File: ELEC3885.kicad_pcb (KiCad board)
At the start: 2 copper layers, 138 x 72 mm, 35 parts, among them J1 MicInstIn, J2 LineIn, J3 HeadPhoneOut, J4 LineOutR, J5 LineOutL, J6 Conn_01x24_Female, J7 Conn_01x24_Female, U1 AP7313, U2 SGTL5000XNLA3, U3 Teensy4.1

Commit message: Initial schematic complete
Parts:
- added J8: Conn_01x06_Female, Connector_PinSocket_2.54mm:PinSocket_2x03_P2.54mm_Vertical, F.Cu at (97.3, 111.3)
- added J9: Conn_01x05_Female, Connector_PinSocket_2.54mm:PinSocket_1x05_P2.54mm_Vertical, F.Cu at (90.0, 83.0)
- added SW1: SW_Push, Button_Switch_SMD:SW_Push_1P1T_NO_6x6mm_H9.5mm, F.Cu at (117.5, 142.8)
- added SW2: SW_Push, Button_Switch_SMD:SW_Push_1P1T_NO_6x6mm_H9.5mm, F.Cu at (106.5, 142.8)
- added SW3: SW_Push, Button_Switch_SMD:SW_Push_1P1T_NO_6x6mm_H9.5mm, F.Cu at (95.6, 142.8)
- added SW4: SW_Push, Button_Switch_SMD:SW_Push_1P1T_NO_6x6mm_H9.5mm, F.Cu at (84.6, 142.8)
- U3: footprint teensy:Teensy41_no_extras -> teensy:Teensy41
- moved J1 40.9 mm to (82.0, 117.6), turned to 180 degrees
- moved H3 9.50 mm to (203.0, 141.5)
- moved H4 9.50 mm to (75.0, 141.5)
- moved U1 5.75 mm to (132.2, 110.3), turned to 90 degrees
- moved FB1 4.62 mm to (126.4, 108.6), turned to 180 degrees
- moved C10 3.03 mm to (125.0, 110.0)
- moved C7 2.09 mm to (127.2, 110.4), turned to -90 degrees
- moved C3 1.95 mm to (132.2, 107.4), turned to 180 degrees
- moved R1 1.25 mm to (130.9, 121.8)
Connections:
- net Net-(J7-Pad21) renamed /Teensy/BUTTON_0
- net Net-(J7-Pad22) renamed /Teensy/BUTTON_1
- net Net-(J7-Pad23) renamed /Teensy/BUTTON_2
- net Net-(J7-Pad24) renamed /Teensy/BUTTON_3
- J1 pad 1: unconnected-(J1-Pad1) -> GND
- J1 pad 2: unconnected-(J1-Pad2) -> Net-(J1-Pad2)
- J1 pad 3: unconnected-(J1-Pad3) -> Net-(J1-Pad3)
- J2 pad RN: GND -> /Audio/MEMS_IN
- J2 pad TN: GND -> /Audio/MEMS_IN
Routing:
- net +3.3V: track 180.5 -> 268.3 mm, vias 5 -> 10
- net /Teensy/BUTTON_3: track 8.92 -> 68.6 mm, vias 0 -> 1
- net /Teensy/BUTTON_2: track 8.92 -> 60.1 mm, vias 0 -> 1
- net /Teensy/BUTTON_1: track 8.92 -> 51.9 mm, vias 0 -> 1
- net /Audio/MEMS_IN: track 0.00 -> 40.5 mm
- net /Teensy/BUTTON_0: track 8.92 -> 43.2 mm, vias 0 -> 1
- net GND: track 11.8 -> 44.9 mm, vias 9 -> 13
- net /Audio/MIC_IN: track 13.0 -> 37.9 mm
- net /Audio/HP_VGND: track 73.1 -> 93.8 mm
- net /Audio/LINE_OUT_L: track 51.6 -> 67.5 mm, vias 2 -> 0
- net /Audio/VOLUME_CONTROL: track 84.9 -> 100.7 mm
- net Net-(J1-Pad2): track 0.00 -> 12.6 mm
- net Net-(J1-Pad3): track 0.00 -> 9.36 mm
- net /Audio/LINE_IN_L: track 46.2 -> 54.0 mm
- net /Audio/LINE_IN_R: track 50.8 -> 55.3 mm
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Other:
- board size 138 x 72 mm -> 138 x 81.5 mm
- board text added: "+"
- board text added: "+3.3"
- board text added: "+3.3V"
- board text added: "-"
- board text added: "BCLK"
- board text added: "D In"
- board text added: "D Out"
- board text added: "ECM"
- board text added: "GND"
- board text added: "HP Out"
- board text added: "In"
- board text added: "LCLK"
- board text added: "Line In"
- board text added: "Line Out L"
- board text added: "Line Out R"
- board text added: "MCLK"
- board text added: "MEMS"
- board text added: "MEMS In"
- board text added: "Mic In"
- board text added: "Mic In Breakout"
- board text added: "SCL"
- board text added: "SDA"
- board text added: "SW1"
- board text added: "SW2"
- board text added: "SW3"
- board text added: "SW4"
- board text added: "TEENSY 4.1"
- board text added: "Volume"

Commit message: New Revision
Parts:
- J8: footprint Connector_PinSocket_2.54mm:PinSocket_2x03_P2.54mm_Vertical -> Connector_PinSocket_2.54mm:PinSocket_1x06_P2.54mm_Vertical
- moved SW4 106.5 mm to (163.8, 71.5), turned to 90 degrees
- moved SW3 105.0 mm to (172.8, 71.5), turned to 90 degrees
- moved SW2 103.6 mm to (181.8, 71.5), turned to 90 degrees
- moved SW1 102.2 mm to (190.8, 71.5), turned to 90 degrees
- moved J2 82.1 mm to (84.7, 144.2), turned to 180 degrees
- moved J6 60.8 mm to (193.9, 83.6), turned to 0 degrees
- moved J3 40.1 mm to (132.5, 70.9)
- moved J4 39.9 mm to (82.6, 81.5)
- moved J5 39.9 mm to (105.8, 81.7)
- moved RV1 38.6 mm to (147.8, 78.5)
- moved J9 34.8 mm to (81.7, 116.7), turned to 90 degrees
- moved J7 34.1 mm to (160.8, 142.0), turned to 180 degrees
- moved J1 32.1 mm to (109.3, 134.4), turned to -90 degrees
- moved C14 15.9 mm to (134.4, 137.5)
- moved C6 15.9 mm to (135.5, 122.3)
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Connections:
- J1 pad 1: GND -> Net-(J1-Pad1)
- J1 pad 3: Net-(J1-Pad3) -> GND
- J7 pad 12: /Audio/VOLUME_CONTROL -> Net-(J7-Pad12)
- J7 pad 19: Net-(J7-Pad19) -> /Audio/VOLUME_CONTROL
- J8 pad 3: Net-(J1-Pad3) -> Net-(J1-Pad1)
- U3 pad 30: Net-(J7-Pad19) -> /Audio/VOLUME_CONTROL
- U3 pad 37: /Audio/VOLUME_CONTROL -> Net-(J7-Pad12)
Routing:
- net /Audio/VOLUME_CONTROL: track 100.7 -> 37.6 mm
- net +3.3V: track 268.3 -> 219.0 mm, vias 10 -> 4
- net /Audio/LINE_OUT_R: track 32.5 -> 78.4 mm
- net /Teensy/BUTTON_3: track 68.6 -> 25.2 mm, vias 1 -> 0
- net /Audio/MCLK: track 64.9 -> 26.8 mm, vias 2 -> 0
- net /Audio/BCLK: track 68.0 -> 32.6 mm
- net /Audio/LCLK: track 67.8 -> 35.0 mm, vias 2 -> 0
- net /Audio/SCL: track 64.5 -> 32.4 mm, vias 2 -> 0
- net /Teensy/BUTTON_2: track 60.1 -> 29.1 mm, vias 1 -> 0
- net /Audio/SDA: track 59.8 -> 33.3 mm
- net /Audio/HP_VGND: track 93.8 -> 71.7 mm, vias 0 -> 2
- net /Audio/MEMS_IN: track 40.5 -> 21.6 mm
- net /Teensy/BUTTON_1: track 51.9 -> 34.0 mm, vias 1 -> 0
- net /Audio/LINE_OUT_L: track 67.5 -> 51.7 mm
- net /Audio/HP_L: track 80.7 -> 66.5 mm
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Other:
- board text added: "Headphone Out"
- board text added: "MEMS Breakout"
- board text removed: "Line In"
- board text removed: "MEMS"
- board text removed: "TEENSY 4.1"

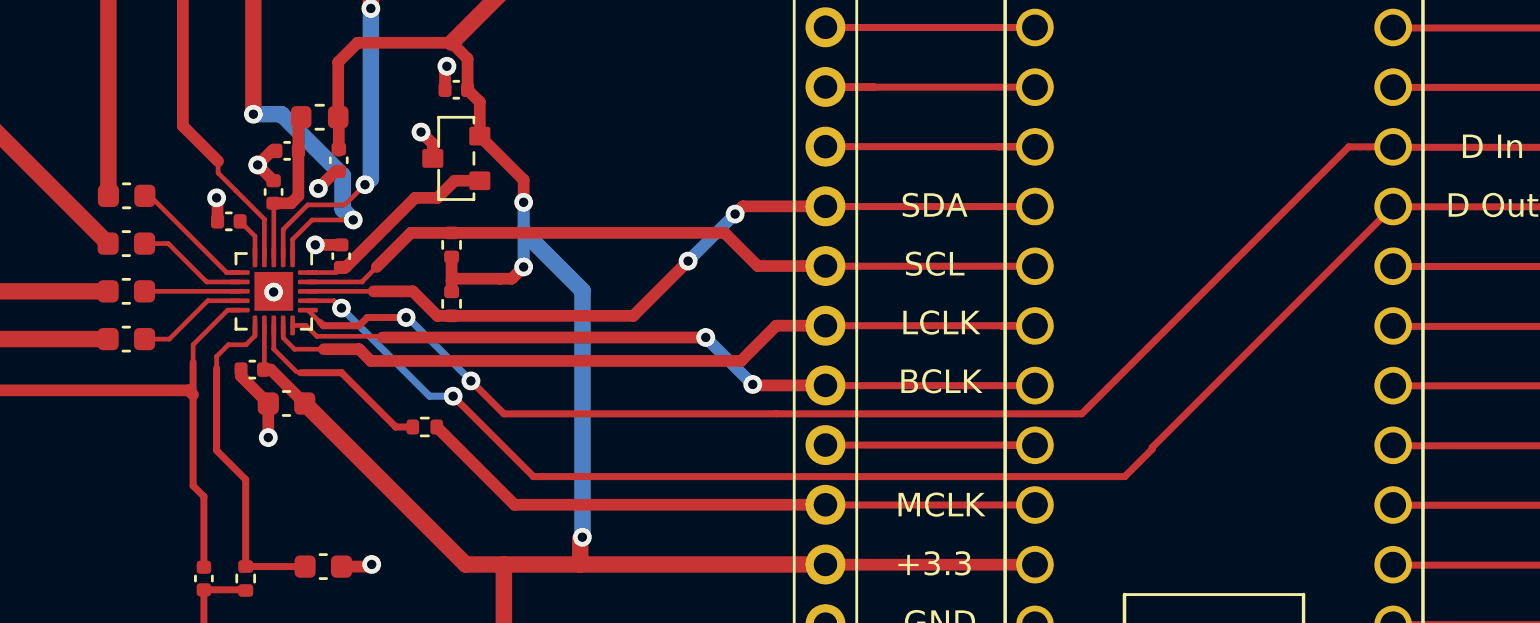
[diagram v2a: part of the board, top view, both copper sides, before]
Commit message: Increase track widths
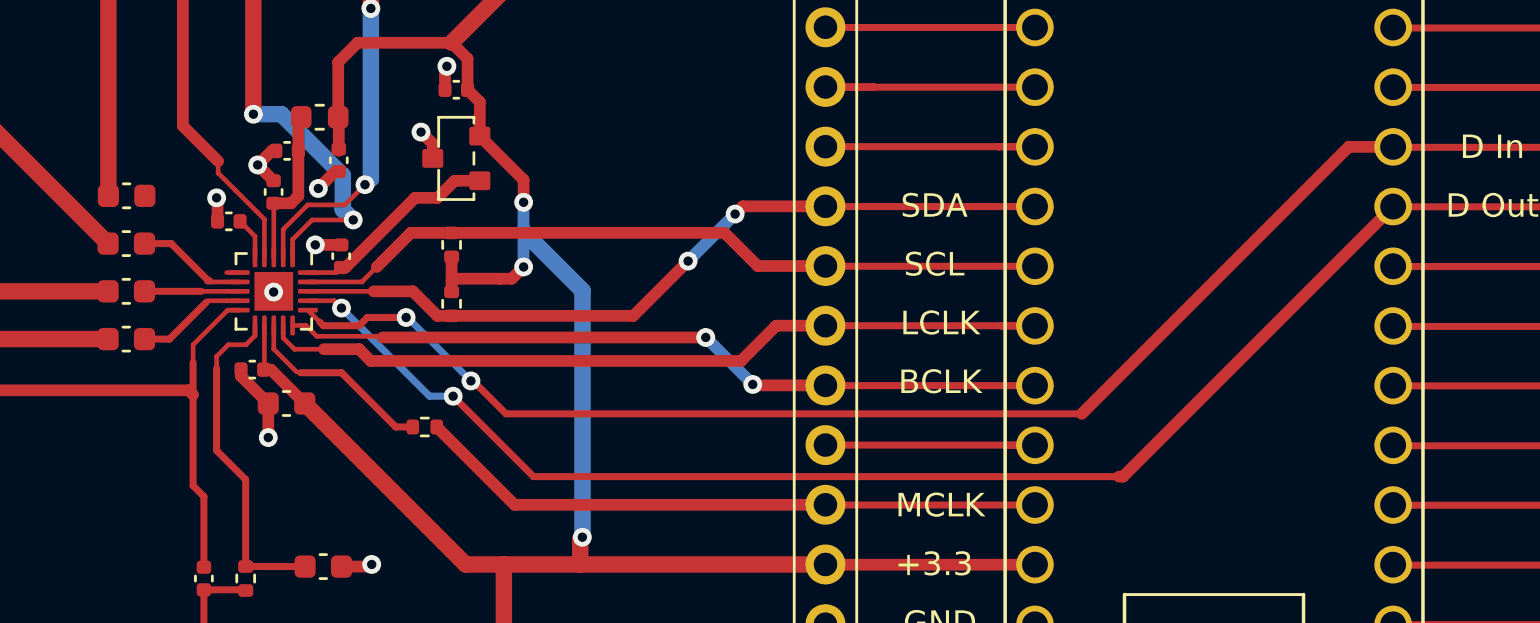
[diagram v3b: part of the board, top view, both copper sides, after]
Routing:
- net Net-(C11-Pad1): track 5.39 -> 0.77 mm
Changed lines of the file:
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@@
   (segment (start 91.75 121) (end 79.25 133.5) (width 0.7) (layer "F.Cu") (net 3))
   (segment (start 130.318 125.288) (end 124.038 125.288) (width 0.7) (layer "F.Cu") (net 3))
-  (segment (start 135.919 125.288) (end 131.868 125.288) (width 0.2) (layer "F.Cu") (net 4))
+  (segment (start 135.919 125.288) (end 134.288 125.288) (width 0.2) (layer "F.Cu") (net 4))
+  (segment (start 131.868 125.288) (end 134.288 125.288) (width 0.3) (layer "F.Cu") (net 4))
   (segment (start 111 139.75) (end 93.75 139.75) (width 0.7) (layer "F.Cu") (net 5))
   (segment (start 93.75 139.75) (end 90.35 136.35) (width 0.7) (layer "F.Cu") (net 5))
@@
   (segment (start 123.43 127.32) (end 111 139.75) (width 0.7) (layer "F.Cu") (net 5))
   (segment (start 130.318 127.32) (end 123.43 127.32) (width 0.7) (layer "F.Cu") (net 5))
-  (segment (start 134.557 125.688) (end 132.925 127.32) (width 0.2) (layer "F.Cu") (net 6))
+  (segment (start 131.868 127.32) (end 132.93 127.32) (width 0.3) (layer "F.Cu") (net 6))
   (segment (start 135.919 125.688) (end 134.557 125.688) (width 0.2) (layer "F.Cu") (net 6))
-  (segment (start 132.925 127.32) (end 131.868 127.32) (width 0.2) (layer "F.Cu") (net 6))
+  (segment (start 132.93 127.32) (end 134.5 125.75) (width 0.3) (layer "F.Cu") (net 6))
   (segment (start 136.569 123.838) (end 136.569 122.944) (width 0.2) (layer "F.Cu") (net 7))
   (segment (start 136.569 122.944) (end 135.935 122.31) (width 0.2) (layer "F.Cu") (net 7))
@@
   (segment (start 132.099 121.224) (end 131.881 121.224) (width 0.2) (layer "F.Cu") (net 10))
   (segment (start 135.919 124.488) (end 135.363 124.488) (width 0.2) (layer "F.Cu") (net 10))
-  (segment (start 135.363 124.488) (end 132.099 121.224) (width 0.2) (layer "F.Cu") (net 10))
   (segment (start 130.318 123.256) (end 105.758876 98.696876) (width 0.7) (layer "F.Cu") (net 11))
   (segment (start 105.758876 98.696876) (end 105.758876 81.746207) (width 0.7) (layer "F.Cu") (net 11))
@@
   (segment (start 140.25 128.75) (end 138.5 128.75) (width 0.3) (layer "F.Cu") (net 50))
   (segment (start 138.335 128.71) (end 137.369 127.744) (width 0.2) (layer "F.Cu") (net 50))
+  (segment (start 147.25 130.5) (end 171.75 130.5) (width 0.3) (layer "F.Cu") (net 51))
   (segment (start 185 119.16) (end 193.905 119.16) (width 0.3) (layer "F.Cu") (net 51))
-  (segment (start 183.11 119.14) (end 172 130.25) (width 0.3) (layer "F.Cu") (net 51))
-  (segment (start 172 130.25) (end 171.75 130.5) (width 0.3) (layer "F.Cu") (net 51))
+  (segment (start 185 119.14) (end 183.11 119.14) (width 0.5) (layer "F.Cu") (net 51))
+  (segment (start 183.11 119.14) (end 171.75 130.5) (width 0.5) (layer "F.Cu") (net 51))
   (segment (start 138.819 126.088) (end 139.33148 126.60048) (width 0.2) (layer "F.Cu") (net 51))
-  (segment (start 185 119.14) (end 183.11 119.14) (width 0.3) (layer "F.Cu") (net 51))
-  (segment (start 147.159349 130.5) (end 145.758849 129.0995) (width 0.3) (layer "F.Cu") (net 51))
-  (segment (start 158.75 130.5) (end 147.159349 130.5) (width 0.3) (layer "F.Cu") (net 51))
   (segment (start 141 126.75) (end 139.481 126.75) (width 0.3) (layer "F.Cu") (net 51))
+  (segment (start 145.758849 129.0995) (end 145.8495 129.0995) (width 0.3) (layer "F.Cu") (net 51))
+  (segment (start 145.8495 129.0995) (end 147.25 130.5) (width 0.3) (layer "F.Cu") (net 51))
   (segment (start 143 126.4005) (end 141.3495 126.4005) (width 0.3) (layer "F.Cu") (net 51))
-  (segment (start 171.75 130.5) (end 158.75 130.5) (width 0.3) (layer "F.Cu") (net 51))
   (segment (start 141.3495 126.4005) (end 141 126.75) (width 0.3) (layer "F.Cu") (net 51))
   (segment (start 139.481 126.75) (end 139.33148 126.60048) (width 0.3) (layer "F.Cu") (net 51))
@@
   (segment (start 143.159349 126.5) (end 143 126.5) (width 0.3) (layer "B.Cu") (net 51))
   (segment (start 139.938 125.688) (end 140.25 126) (width 0.2) (layer "F.Cu") (net 52))
-  (segment (start 174.75 132) (end 173.579511 133.170489) (width 0.3) (layer "F.Cu") (net 52))
+  (segment (start 173.329511 133.170489) (end 173.579511 133.170489) (width 0.3) (layer "F.Cu") (net 52))
   (segment (start 193.915 121.69) (end 185.01 121.69) (width 0.3) (layer "F.Cu") (net 52))
-  (segment (start 148.420489 133.170489) (end 145 129.75) (width 0.3) (layer "F.Cu") (net 52))
-  (segment (start 185.01 121.69) (end 185 121.68) (width 0.3) (layer "F.Cu") (net 52))
-  (segment (start 173.579511 133.170489) (end 148.420489 133.170489) (width 0.3) (layer "F.Cu") (net 52))
+  (segment (start 148.420489 133.170489) (end 173.329511 133.170489) (width 0.3) (layer "F.Cu") (net 52))
+  (segment (start 145 129.75) (end 148.420489 133.170489) (width 0.3) (layer "F.Cu") (net 52))
+  (segment (start 173.509511 133.170489) (end 173.329511 133.170489) (width 0.5) (layer "F.Cu") (net 52))
+  (segment (start 185 121.68) (end 173.509511 133.170489) (width 0.5) (layer "F.Cu") (net 52))
   (segment (start 138.819 125.688) (end 139.938 125.688) (width 0.2) (layer "F.Cu") (net 52))
-  (segment (start 185 121.68) (end 174.75 131.93) (width 0.3) (layer "F.Cu") (net 52))
-  (segment (start 174.75 131.93) (end 174.75 132) (width 0.3) (layer "F.Cu") (net 52))
+  (segment (start 173.579511 133.100489) (end 173.579511 133.170489) (width 0.3) (layer "F.Cu") (net 52))
   (via (at 140.25 126) (size 0.8) (drill 0.4) (layers "F.Cu" "B.Cu") (net 52))
   (via (at 145 129.75) (size 0.8) (drill 0.4) (layers "F.Cu" "B.Cu") (net 52))
@@
   (segment (start 156.75 93.75) (end 159.27 96.27) (width 0.5) (layer "F.Cu") (net 53))
   (segment (start 150.25 78.475) (end 152.475 76.25) (width 0.5) (layer "F.Cu") (net 53))
-  (segment (start 132.881 123.256) (end 131.868 123.256) (width 0.2) (layer "F.Cu") (net 54))
-  (segment (start 134.513 124.888) (end 132.881 123.256) (width 0.2) (layer "F.Cu") (net 54))
+  (segment (start 134.58848 124.83848) (end 134.638 124.83848) (width 0.3) (layer "F.Cu") (net 54))
+  (segment (start 131.868 123.256) (end 133.006 123.256) (width 0.3) (layer "F.Cu") (net 54))
+  (segment (start 133.006 123.256) (end 134.58848 124.83848) (width 0.3) (layer "F.Cu") (net 54))
   (segment (start 135.919 124.888) (end 134.513 124.888) (width 0.2) (layer "F.Cu") (net 54))
   (segment (start 134.395 140.81) (end 134.395 137.988) (width 0.3) (layer "F.Cu") (net 55))

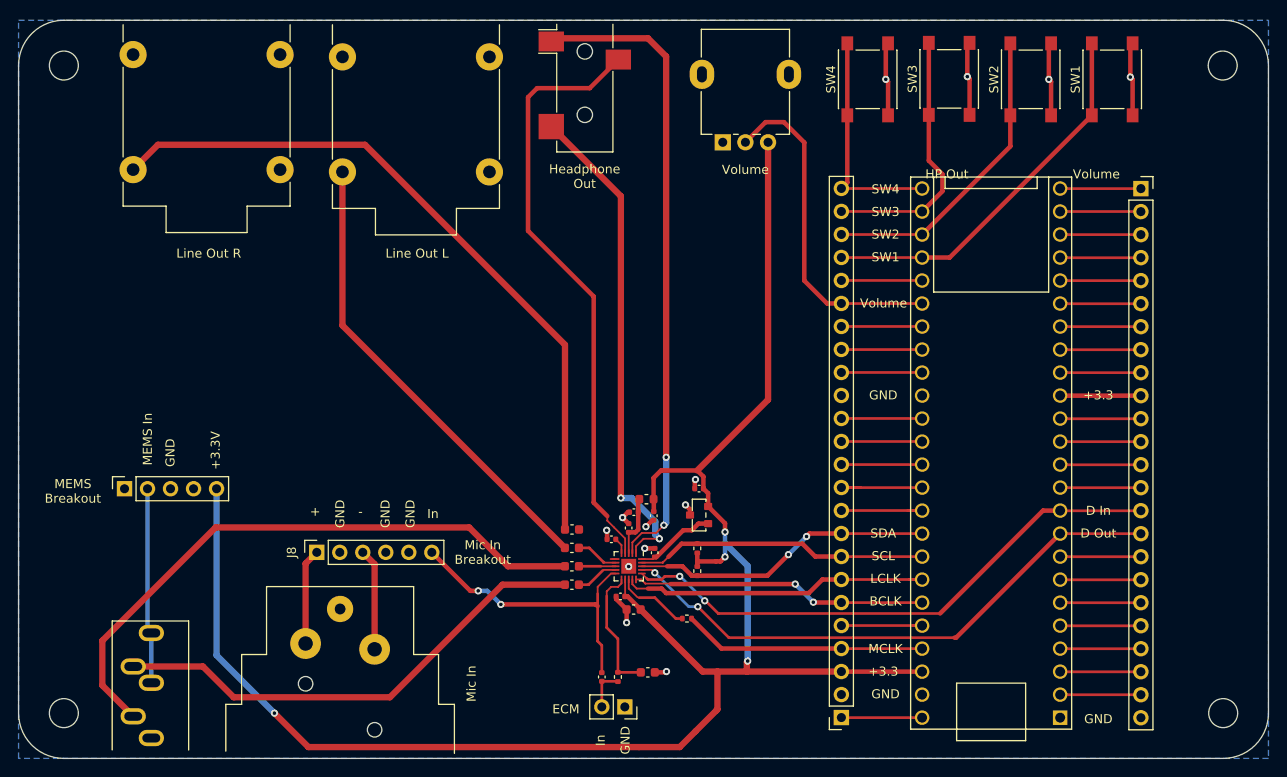
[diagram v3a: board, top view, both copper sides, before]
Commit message: Fab cleanup, trace tapers added
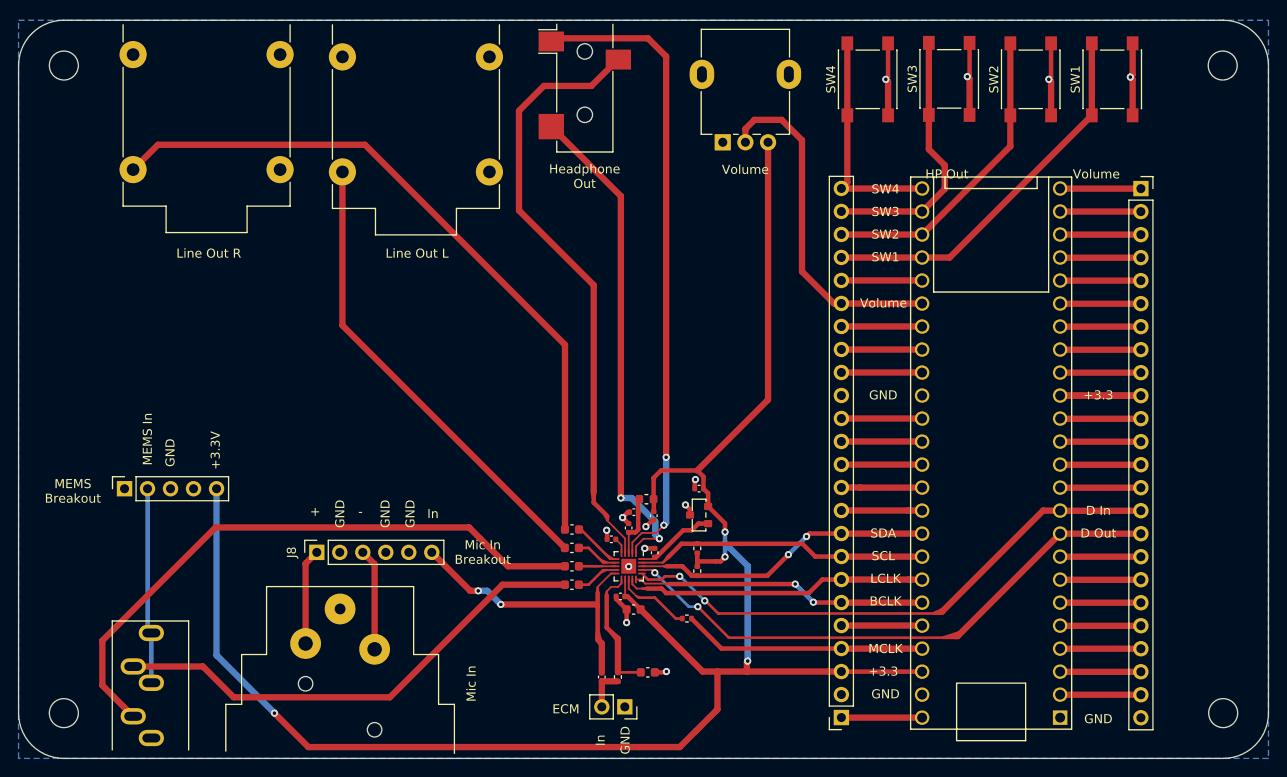
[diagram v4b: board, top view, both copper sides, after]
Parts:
- C8: value 0.1uF -> .1uF
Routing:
- net /Audio/HP_L: track 66.5 -> 88.5 mm
- net Net-(C11-Pad1): track 0.77 -> 5.61 mm
- net Net-(J7-Pad5): track 10.1 -> 8.92 mm
- net GND: track 44.9 -> 46.0 mm
- net /Audio/VOLUME_CONTROL: track 37.6 -> 38.3 mm
